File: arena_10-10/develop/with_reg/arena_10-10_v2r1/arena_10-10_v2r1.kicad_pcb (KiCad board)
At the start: 6 copper layers, 248.9 x 228.6 mm, 538 parts, among them J1 Cetus RJ45 Magjack, J10 Conn_01x05, J100 PinSocket_1x24_P2.54mm_Vertic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, J101 PinSocket_1x24_P2.54mm_Vertic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, J102 PinSocket_2x03_P2.00mm_Vertic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, J11 Conn_01x05, J12 Conn_01x05, J13 Conn_01x05, J14 Conn_01x05, J15 Conn_01x05, J16 Conn_01x05, J17 Conn_01x05, J18 Conn_01x05, J19 Conn_01x05, J2 Conn_01x02, J20 Conn_01x05, J21 Conn_01x05, J22 Conn_01x05, J23 Conn_01x05, J24 Conn_01x05, J25 Barrel_Jack, J26 XT30 Female, J27 Conn_Coaxial, J28 Conn_Coaxial, J29 Conn_Coaxial, J3 Conn_Coaxial, J30 Conn_01x02, J4 Conn_Coaxial, J5 Conn_01x05, J6 Conn_01x05, J7 Conn_01x05, J8 Conn_01x05, J9 Conn_01x05, P1 NA, P10 NA, P2 NA, P3 NA, P4 NA, P5 NA, P6 NA, P7 NA, P8 NA, P9 NA, SW1 SW_SPDT, U1 Teensy4.1, U10 74LVC2G17, U100 74LVC1G125, U101 74LVC2G17, U102 SN74HCS08, U103 SN74HCS08, U104 74LVC1G125, U105 74LVC2G17, U106 SN74HCS08, U107 SN74HCS08, U108 74LVC1G125, U109 74LVC2G17, U11 74LVC2G17, U110 NID100-5, U112 74LVC1G125, U113 74LVC2G17, U116 74LVC1G125, U117 74LVC2G17, U12 74LVC2G17, U120 74LVC1G125, U121 74LVC2G17, U124 74LVC1G125, U125 74LVC2G17, U13 74LVC2G17, U14 74LVC2G17, U15 74LVC2G17, U16 74LVC2G17, U17 74LVC2G17, U18 74LVC2G17, U19 74LVC2G17, U2 SN74LVC1T45DBV, U20 74LVC2G17, U21 74LVC2G17, U22 74LVC2G17, U23 74LVC2G17, U24 74LVC2G17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

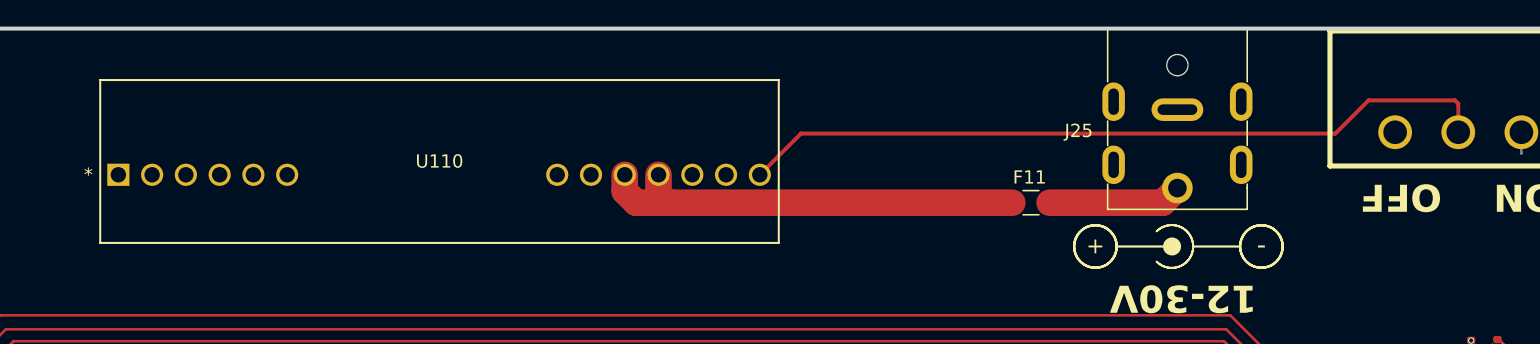
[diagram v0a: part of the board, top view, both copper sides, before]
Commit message: Added zones around NID100-5 and jack.
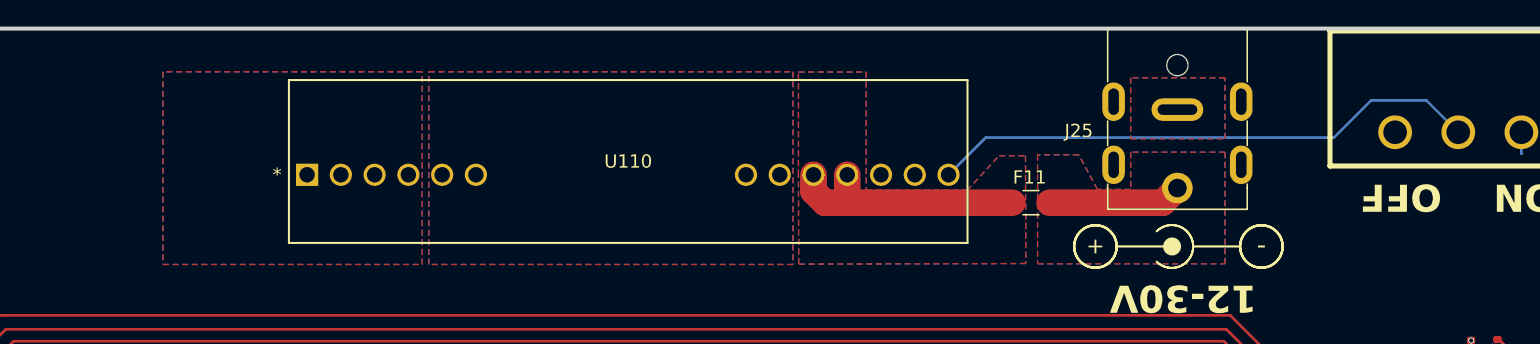
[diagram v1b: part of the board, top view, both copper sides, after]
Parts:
- F11: value T 5A 63V -> T 7A 63V
- moved U110 14.2 mm to (169.0, 74.5)
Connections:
- net Net-(F11-Pad2) renamed /Power/VJACK
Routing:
- net Net-(SW1-B): track 57.5 -> 42.0 mm
- net /Power/VPWR: track 31.9 -> 17.7 mm
- added copper zone on B.Cu, net +5V
- added copper zone on F.Cu, net +5V
- added copper zone on B.Cu, net /Power/VJACK
- added copper zone on F.Cu, net /Power/VJACK
- added copper zone on B.Cu, net /Power/VPWR
- added copper zone on F.Cu, net /Power/VPWR
- added copper zone on B.Cu, net GND
- added copper zone on F.Cu, net GND
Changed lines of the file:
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@@
 			(keep_end_layers yes)
 			(zone_layer_connections)
-			(net "Net-(F11-Pad2)")
+			(net "/Power/VJACK")
 			(pintype "passive")
 		)
@@
 			)
 		)
-		(property "Value" "T 5A 63V"
+		(property "Value" "T 7A 63V"
 			(at 0 1.83 0)
 			(layer "User.2")
@@
 			)
 		)
-		(property "LCSC Part #" "C1972666"
+		(property "LCSC Part #" "C1972821"
 			(at 0 0 0)
 			(unlocked yes)
@@
 			(layers "F.Cu" "F.Mask" "F.Paste")
 			(roundrect_rratio 0.2)
-			(net "Net-(F11-Pad2)")
+			(net "/Power/VJACK")
 			(pintype "passive")
 		)
@@
 	(footprint "NID100-5:NID100_MWU"
 		(layer "F.Cu")
-		(at 154.839999 74.500001)
+		(at 169.039454 74.500001)
 		(tags "NID100-5 ")
 		(property "Reference" "U110"
@@
 	)
 	(segment
-		(start 255.4 68.9)
-		(end 255.6498 69.1498)
-		(width 0.3)
-		(layer "F.Cu")
-		(net "Net-(SW1-B)")
-	)
-	(segment
-		(start 246.4 71.4)
-		(end 248.9 68.9)
+		(start 255.4 71.0502)
+		(end 255.6498 71.3)
 		(width 0.3)
 		(layer "F.Cu")
@@
 	)
 	(segment
-		(start 203.1 74.500001)
-		(end 206.200001 71.4)
-		(width 0.3)
-		(layer "F.Cu")
+		(start 246.3 71.7)
+		(end 249.1 68.9)
+		(width 0.2)
+		(layer "B.Cu")
 		(net "Net-(SW1-B)")
 	)
 	(segment
-		(start 206.200001 71.4)
-		(end 246.4 71.4)
-		(width 0.3)
-		(layer "F.Cu")
+		(start 249.1 68.9)
+		(end 253.2498 68.9)
+		(width 0.2)
+		(layer "B.Cu")
 		(net "Net-(SW1-B)")
 	)
 	(segment
-		(start 248.9 68.9)
-		(end 255.4 68.9)
-		(width 0.3)
-		(layer "F.Cu")
+		(start 253.2498 68.9)
+		(end 255.6498 71.3)
+		(width 0.2)
+		(layer "B.Cu")
 		(net "Net-(SW1-B)")
 	)
 	(segment
-		(start 255.6498 69.1498)
-		(end 255.6498 71.3)
-		(width 0.3)
-		(layer "F.Cu")
+		(start 220.099456 71.7)
+		(end 246.3 71.7)
+		(width 0.2)
+		(layer "B.Cu")
 		(net "Net-(SW1-B)")
 	)
 	(segment
-		(start 255.4 71.0502)
-		(end 255.6498 71.3)
-		(width 0.3)
-		(layer "F.Cu")
+		(start 217.299455 74.500001)
+		(end 220.099456 71.7)
+		(width 0.2)
+		(layer "B.Cu")
 		(net "Net-(SW1-B)")
 	)
@@
 	)
 	(segment
-		(start 233.42 76.6)
-		(end 224.9 76.6)
-		(width 2)
-		(layer "F.Cu")
-		(net "Net-(F11-Pad2)")
-	)
-	(segment
-		(start 234.52 75.5)
-		(end 233.42 76.6)
-		(width 2)
-		(layer "F.Cu")
-		(net "Net-(F11-Pad2)")
-	)
-	(segment
 		(start 294.05 105.7977)
 		(end 291.914 107.9337)
@@
 	)
 	(segment
-		(start 193.8 76.6)
-		(end 192.94 75.74)
+		(start 209.679455 75.679455)
+		(end 209.679455 74.500001)
 		(width 2)
 		(layer "F.Cu")
@@
 	)
 	(segment
-		(start 195.48 75.679455)
-		(end 195.48 74.500001)
+		(start 207.139455 74.500001)
+		(end 207.139455 75.74)
 		(width 2)
 		(layer "F.Cu")
@@
 	)
 	(segment
-		(start 222.1 76.6)
-		(end 196.400545 76.6)
+		(start 207.999455 76.6)
+		(end 222.1 76.6)
 		(width 2)
 		(layer "F.Cu")
@@
 	)
 	(segment
-		(start 192.94 75.74)
-		(end 192.94 74.500001)
-		(width 2)
-		(layer "F.Cu")
-		(net "/Power/VPWR")
-	)
-	(segment
-		(start 196.400545 76.6)
-		(end 193.8 76.6)
+		(start 207.139455 75.74)
+		(end 207.999455 76.6)
 		(width 2)
 		(layer "F.Cu")
@@
 		(net "Net-(R137-Pad1)")
 	)
+	(segment
+		(start 233.42 76.6)
+		(end 224.9 76.6)
+		(width 2)
+		(layer "F.Cu")
+		(net "/Power/VJACK")
+	)
+	(segment
+		(start 234.52 75.5)
+		(end 233.42 76.6)
+		(width 2)
+		(layer "F.Cu")
+		(net "/Power/VJACK")
+	)
 	(zone
 		(layers "F.Cu" "F.Mask" "B.Cu" "B.Mask" "In1.Cu" "F.SilkS" "In2.Cu" "B.SilkS"
@@
 			)
 		)
+	)
+	(zone
+		(net "GND")
+		(layers "F.Cu" "B.Cu")
+		(hatch edge 0.5)
+		(priority 8)
+		(connect_pads
+			(clearance 0)
+		)
+		(min_thickness 0.25)
+		(fill yes
+			(thermal_gap 0.25)
+			(thermal_bridge_width 0.75)
+			(island_removal_mode 0)
+		)
+		(polygon
+			(pts
+				(xy 231 67.2) (xy 231 71.8) (xy 238.1 71.8) (xy 238.1 67.2)
+			)
+		)
+	)
+	(zone
+		(net "GND")
+		(layers "F.Cu" "B.Cu")
+		(hatch edge 0.5)
+		(priority 5)
+		(connect_pads
+			(clearance 0)
+		)
+		(min_thickness 0.25)
+		(fill yes
+			(thermal_gap 0.25)
+			(thermal_bridge_width 0.75)
+			(island_removal_mode 0)
+		)
+		(polygon
+			(pts
+				(xy 178.199455 66.75) (xy 205.599455 66.75) (xy 205.599455 81.25) (xy 178.199455 81.25)
+			)
+		)
+	)
+	(zone
+		(net "+5V")
+		(layers "F.Cu" "B.Cu")
+		(hatch edge 0.5)
+		(priority 4)
+		(connect_pads
+			(clearance 0)
+		)
+		(min_thickness 0.25)
+		(fill yes
+			(thermal_gap 0.25)
+			(thermal_bridge_width 0.75)
+			(island_removal_mode 0)
+		)
+		(polygon
+			(pts
+				(xy 177.699455 66.75) (xy 158.199455 66.75) (xy 158.199455 81.25) (xy 177.699455 81.25)
+			)
+		)
+	)
+	(zone
+		(net "/Power/VPWR")
+		(layers "F.Cu" "B.Cu")
+		(hatch edge 0.5)
+		(priority 6)
+		(connect_pads
+			(clearance 0)
+		)
+		(min_thickness 0.25)
+		(fill yes
+			(thermal_gap 0.25)
+			(thermal_bridge_width 0.75)
+			(island_removal_mode 0)
+		)
+		(polygon
+			(pts
+				(xy 206.005928 74.565317) (xy 206.005928 66.765317) (xy 211.105928 66.765317) (xy 211.105928 75.665317)
+				(xy 218.705928 75.665317) (xy 221.105928 73.065317) (xy 223.089803 73.065317) (xy 223.109811 81.17818)
+				(xy 206.025828 81.221986)
+			)
+		)
+	)
+	(zone
+		(net "/Power/VJACK")
+		(layers "F.Cu" "B.Cu")
+		(hatch edge 0.5)
+		(priority 7)
+		(connect_pads
+			(clearance 0)
+		)
+		(min_thickness 0.25)
+		(fill yes
+			(thermal_gap 0.25)
+			(thermal_bridge_width 0.75)
+			(island_removal_mode 0)
+		)
+		(polygon
+			(pts
+				(xy 224 73) (xy 224 81.2) (xy 238.1 81.2) (xy 238.1 72.8) (xy 231 72.8) (xy 231 75.6) (xy 228.5 75.6)
+				(xy 227.1 73)
+			)
+		)
